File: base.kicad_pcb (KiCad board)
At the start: 2 copper layers, 95 x 95 mm, 4 parts, among them M8 MountingHole_8.4mm_M8

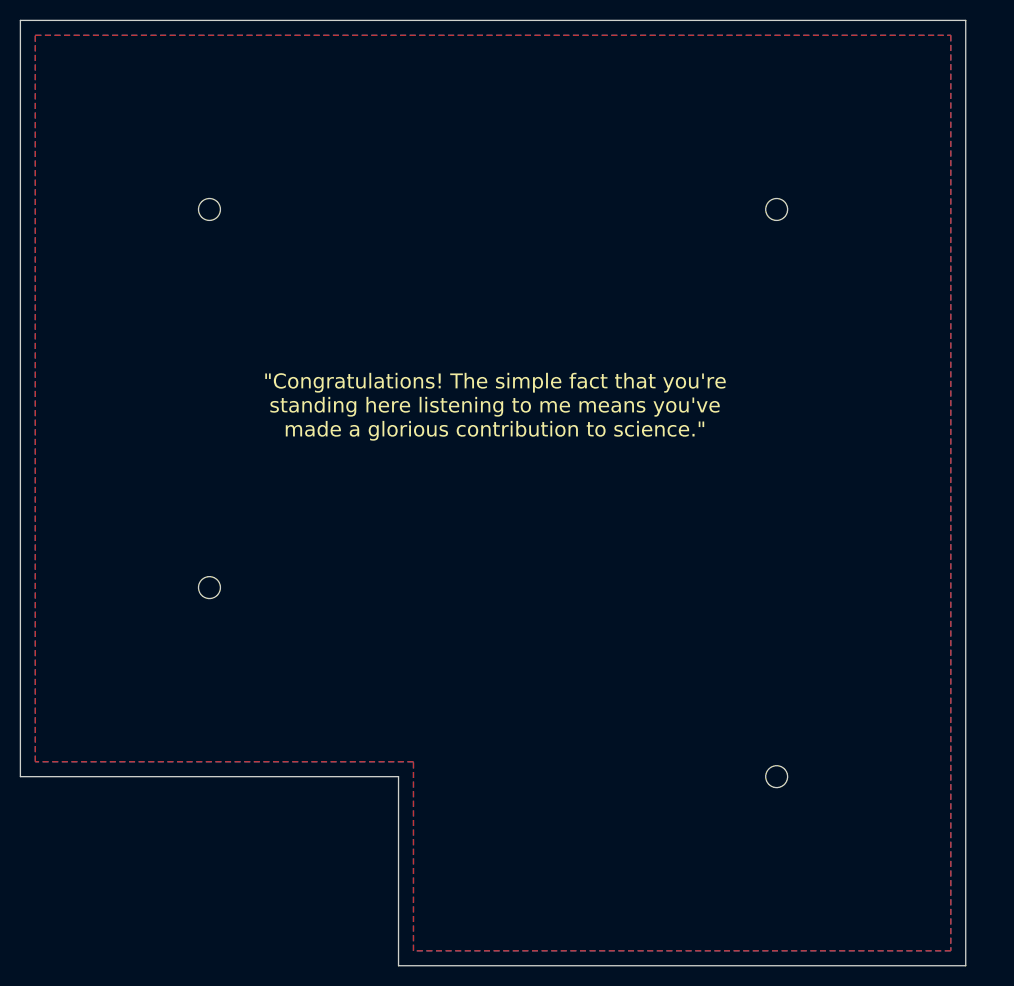
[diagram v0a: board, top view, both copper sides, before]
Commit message: base: Adds OSEG logo and meta-data
* Source (fixed, manual value)
* License (fixed, manual value)
* Version (placeholder, missing replacement method!)
* Version-Date (placeholder, missing replacement method!)
* Manufacturer (fixed, manual value)
* Manufacturer-Serial-Number (placeholder, filled in by manufacturer)
* Batch (fixed, manual value)
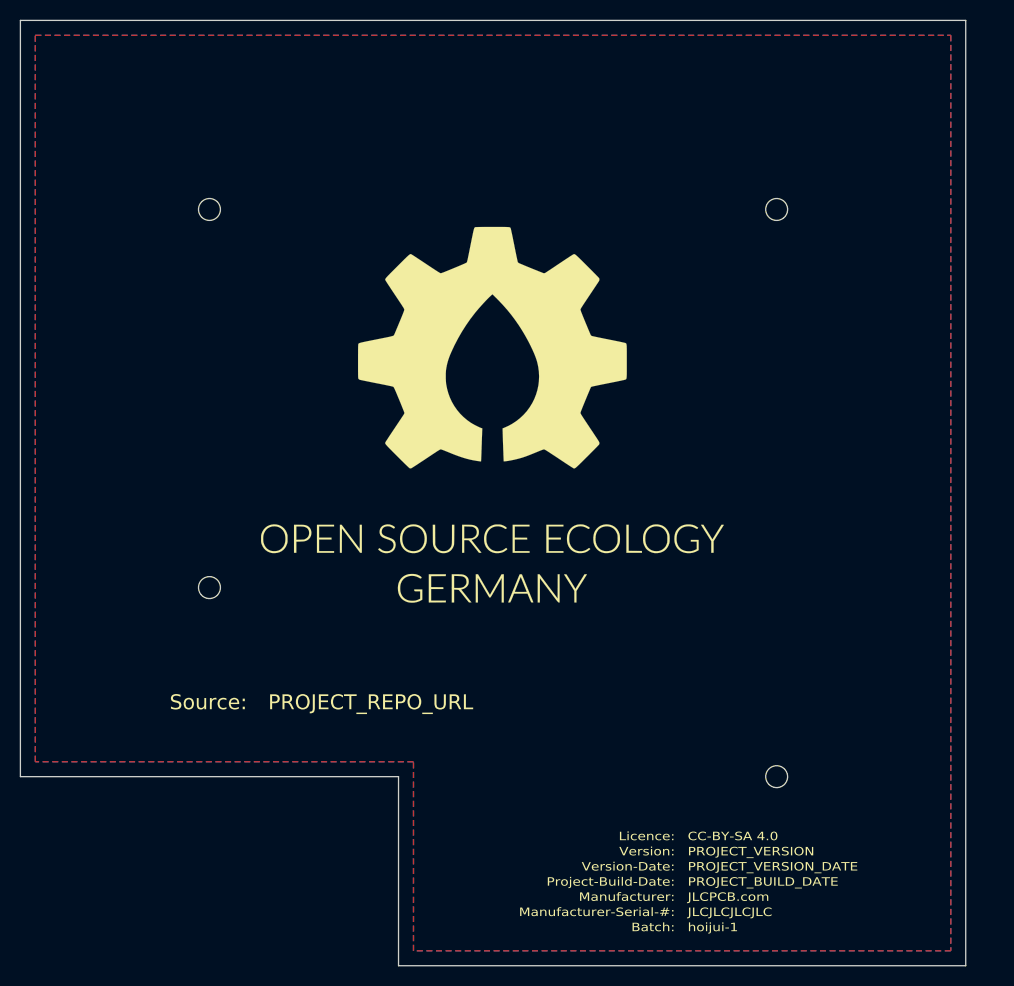
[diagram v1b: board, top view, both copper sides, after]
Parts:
- added G***: LOGO, LOGO, B.Cu at (128.0, 92.7)
- added G***: LOGO, LOGO, F.Cu at (125.7, 88.9)
- added G***: LOGO, LOGO, F.Cu at (126.0, 92.7)
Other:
- rule pad_to_mask_clearance: 0 -> 0.2
- board text added: "Batch:"
- board text added: "CC-BY-SA 4.0"
- board text added: "JLCJLCJLCJLC"
- board text added: "JLCPCB.com"
- board text added: "Licence:"
- board text added: "Manufacturer-Serial-#:"
- board text added: "Manufacturer:"
- board text added: "PROJECT_BUILD_DATE"
- board text added: "PROJECT_REPO_URL"
- board text added: "PROJECT_VERSION"
- board text added: "PROJECT_VERSION_DATE"
- board text added: "Project-Build-Date:"
- board text added: "Source:"
- board text added: "Version-Date:"
- board text added: "Version:"
- board text added: "hoijui-1"
- board text removed: ""Congratulations! The simple fact that you're standing here listening to me means you've made a glorious contribution to science.""

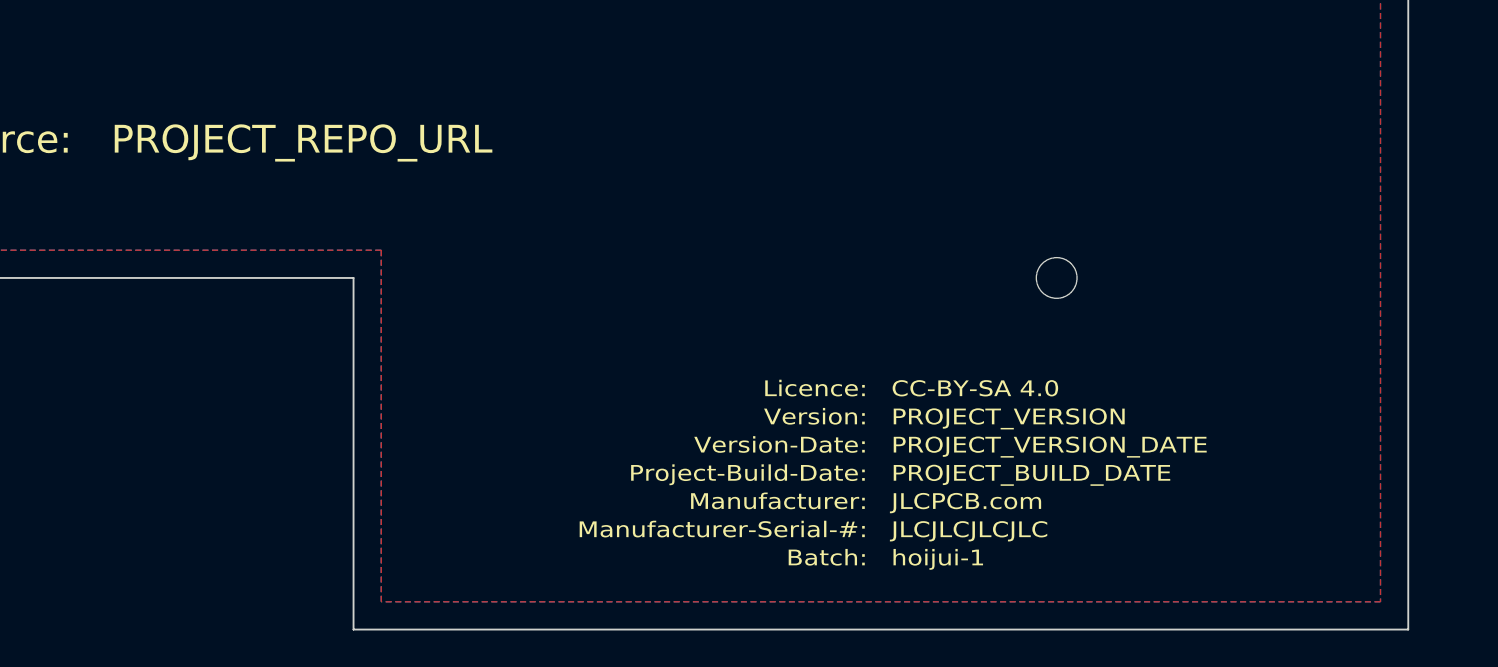
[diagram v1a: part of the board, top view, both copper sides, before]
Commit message: base: Adds more meta-data varables
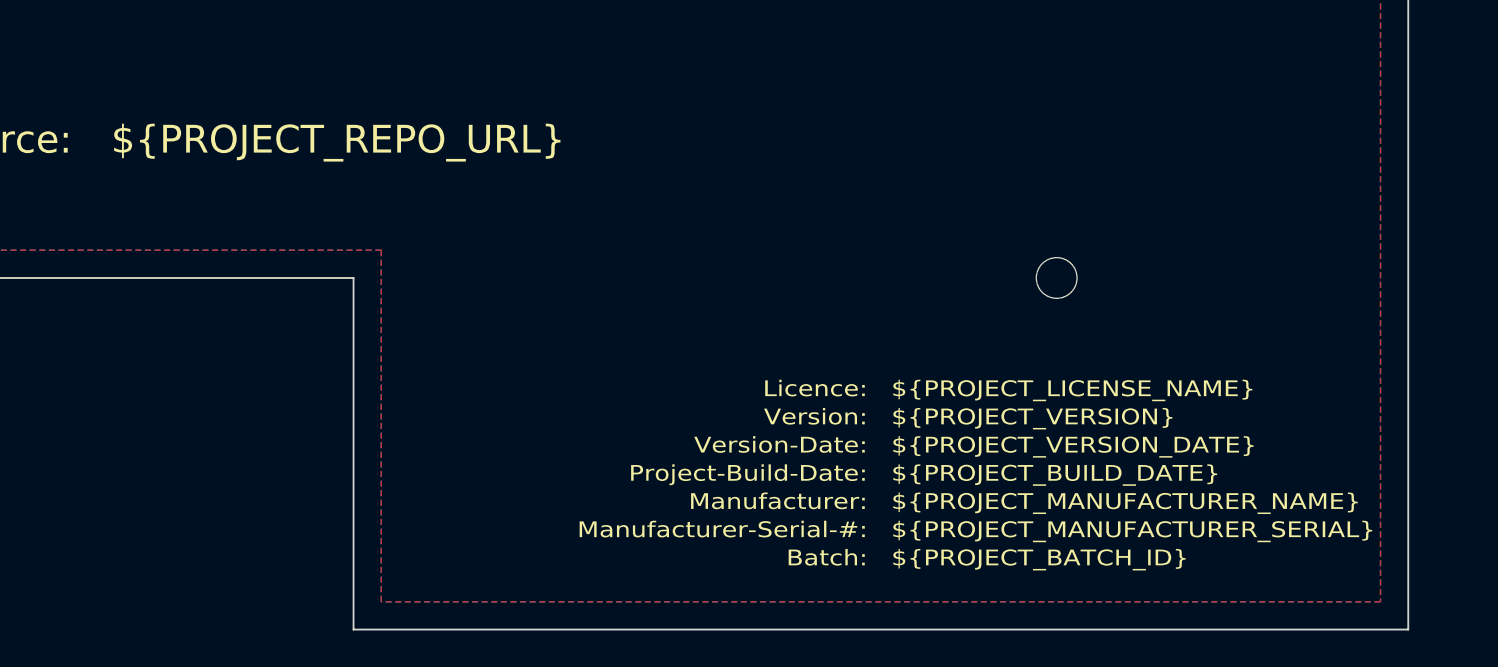
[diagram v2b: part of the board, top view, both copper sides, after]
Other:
- board text added: "${PROJECT_BATCH_ID}"
- board text added: "${PROJECT_BUILD_DATE}"
- board text added: "${PROJECT_LICENSE_NAME}"
- board text added: "${PROJECT_MANUFACTURER_NAME}"
- board text added: "${PROJECT_MANUFACTURER_SERIAL}"
- board text added: "${PROJECT_REPO_URL}"
- board text added: "${PROJECT_VERSION_DATE}"
- board text added: "${PROJECT_VERSION}"
- board text removed: "CC-BY-SA 4.0"
- board text removed: "JLCJLCJLCJLC"
- board text removed: "JLCPCB.com"
- board text removed: "PROJECT_BUILD_DATE"
- board text removed: "PROJECT_REPO_URL"
- board text removed: "PROJECT_VERSION"
- board text removed: "PROJECT_VERSION_DATE"
- board text removed: "hoijui-1"
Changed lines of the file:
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@@
       (xy -7.283727 7.423656) (xy -7.129825 7.419251) (xy -6.975334 7.422964)) (layer F.SilkS) (width 0.01))
   )
-  (gr_text hoijui-1 (at 145.288 135.636) (layer B.SilkS)
+  (gr_text ${PROJECT_BATCH_ID} (at 145.288 135.636) (layer B.SilkS)
     (effects (font (size 0.85 1) (thickness 0.15)) (justify left mirror))
   )
@@
     (effects (font (size 0.85 1) (thickness 0.15)) (justify right mirror))
   )
-  (gr_text hoijui-1 (at 146.558 135.636) (layer F.SilkS)
+  (gr_text ${PROJECT_BATCH_ID} (at 146.558 135.636) (layer F.SilkS)
     (effects (font (size 0.85 1) (thickness 0.15)) (justify left))
   )
@@
     (effects (font (size 0.85 1) (thickness 0.15)) (justify right))
   )
-  (gr_text PROJECT_REPO_URL (at 151.13 113.03) (layer B.SilkS)
+  (gr_text ${PROJECT_REPO_URL} (at 151.13 113.03) (layer B.SilkS)
     (effects (font (size 1.5 1.5) (thickness 0.25)) (justify left mirror))
   )
-  (gr_text PROJECT_REPO_URL (at 104.394 113.03) (layer F.SilkS)
+  (gr_text ${PROJECT_REPO_URL} (at 104.394 113.03) (layer F.SilkS)
     (effects (font (size 1.5 1.5) (thickness 0.25)) (justify left))
   )
-  (gr_text JLCJLCJLCJLC (at 145.288 134.112) (layer B.SilkS)
+  (gr_text ${PROJECT_MANUFACTURER_SERIAL} (at 145.288 134.112) (layer B.SilkS)
     (effects (font (size 0.85 1) (thickness 0.15)) (justify left mirror))
   )
-  (gr_text PROJECT_VERSION_DATE (at 145.288 129.54) (layer B.SilkS)
+  (gr_text ${PROJECT_VERSION_DATE} (at 145.288 129.54) (layer B.SilkS)
     (effects (font (size 0.85 1) (thickness 0.15)) (justify left mirror))
   )
@@
     (effects (font (size 0.85 1) (thickness 0.15)) (justify right mirror))
   )
-  (gr_text PROJECT_VERSION (at 145.288 128.016) (layer B.SilkS)
+  (gr_text ${PROJECT_VERSION} (at 145.288 128.016) (layer B.SilkS)
     (effects (font (size 0.85 1) (thickness 0.15)) (justify left mirror))
   )
-  (gr_text PROJECT_BUILD_DATE (at 145.288 131.064) (layer B.SilkS)
+  (gr_text ${PROJECT_BUILD_DATE} (at 145.288 131.064) (layer B.SilkS)
     (effects (font (size 0.85 1) (thickness 0.15)) (justify left mirror))
   )
-  (gr_text JLCPCB.com (at 145.288 132.588) (layer B.SilkS)
+  (gr_text ${PROJECT_MANUFACTURER_NAME} (at 145.288 132.588) (layer B.SilkS)
     (effects (font (size 0.85 1) (thickness 0.15)) (justify left mirror))
   )
@@
     (effects (font (size 0.85 1) (thickness 0.15)) (justify right mirror))
   )
-  (gr_text "CC-BY-SA 4.0" (at 145.288 126.492) (layer B.SilkS)
+  (gr_text "${PROJECT_LICENSE_NAME}" (at 145.288 126.492) (layer B.SilkS)
     (effects (font (size 0.85 1) (thickness 0.15)) (justify left mirror))
   )
@@
     (effects (font (size 0.85 1) (thickness 0.15)) (justify right mirror))
   )
-  (gr_text PROJECT_BUILD_DATE (at 146.558 131.064) (layer F.SilkS)
+  (gr_text ${PROJECT_BUILD_DATE} (at 146.558 131.064) (layer F.SilkS)
     (effects (font (size 0.85 1) (thickness 0.15)) (justify left))
   )
@@
     (arrow2b (pts (xy 174.5 141.25) (xy 173.373496 141.836421)))
   )
-  (gr_text JLCJLCJLCJLC (at 146.558 134.112) (layer F.SilkS)
+  (gr_text ${PROJECT_MANUFACTURER_SERIAL}  (at 146.558 134.112) (layer F.SilkS)
     (effects (font (size 0.85 1) (thickness 0.15)) (justify left))
   )
-  (gr_text JLCPCB.com (at 146.558 132.588) (layer F.SilkS)
+  (gr_text ${PROJECT_MANUFACTURER_NAME} (at 146.558 132.588) (layer F.SilkS)
     (effects (font (size 0.85 1) (thickness 0.15)) (justify left))
   )
-  (gr_text PROJECT_VERSION_DATE (at 146.558 129.54) (layer F.SilkS)
+  (gr_text ${PROJECT_VERSION_DATE} (at 146.558 129.54) (layer F.SilkS)
     (effects (font (size 0.85 1) (thickness 0.15)) (justify left))
   )
-  (gr_text PROJECT_VERSION (at 146.558 128.016) (layer F.SilkS)
+  (gr_text ${PROJECT_VERSION} (at 146.558 128.016) (layer F.SilkS)
     (effects (font (size 0.85 1) (thickness 0.15)) (justify left))
   )
@@
     (effects (font (size 0.85 1) (thickness 0.15)) (justify right))
   )
-  (gr_text "CC-BY-SA 4.0" (at 146.558 126.492) (layer F.SilkS)
+  (gr_text ${PROJECT_LICENSE_NAME} (at 146.558 126.492) (layer F.SilkS)
     (effects (font (size 0.85 1) (thickness 0.15)) (justify left))
   )

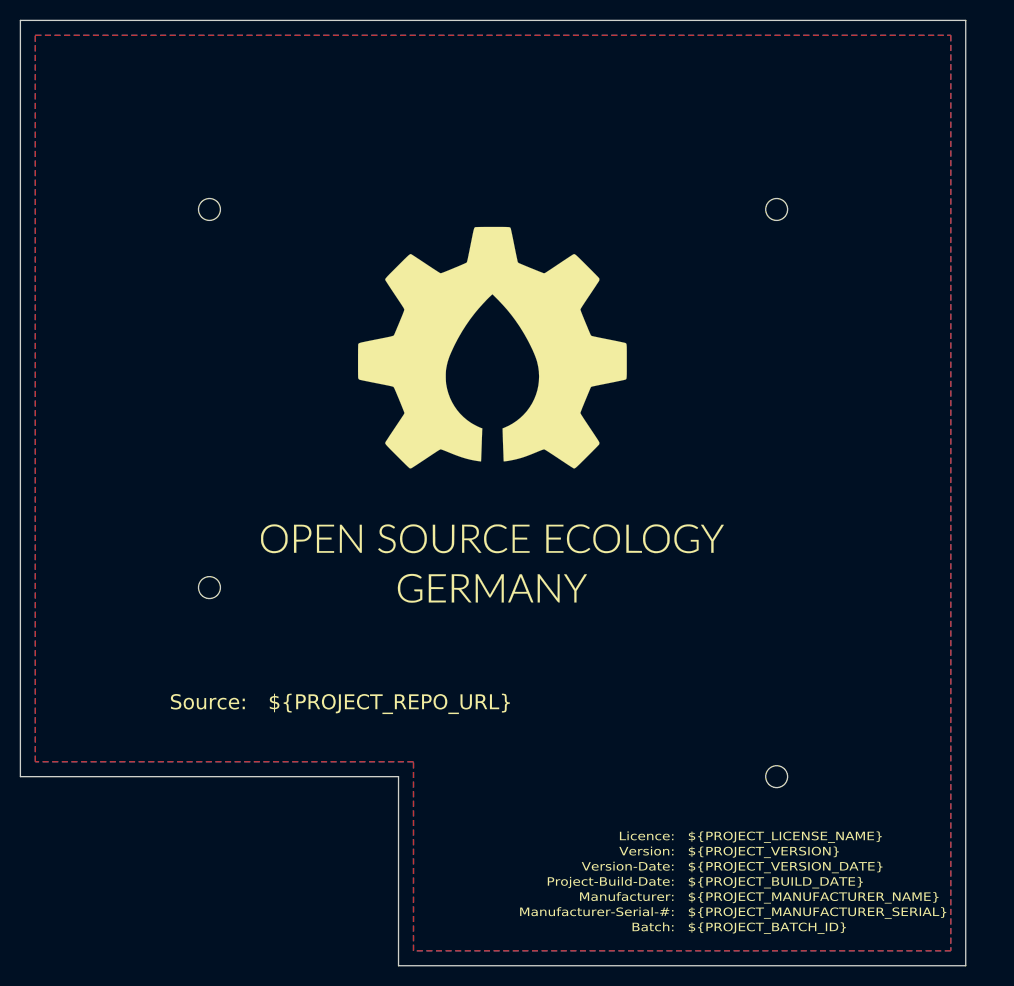
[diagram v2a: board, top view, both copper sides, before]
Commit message: TMP adds 5 rectangles for image injector
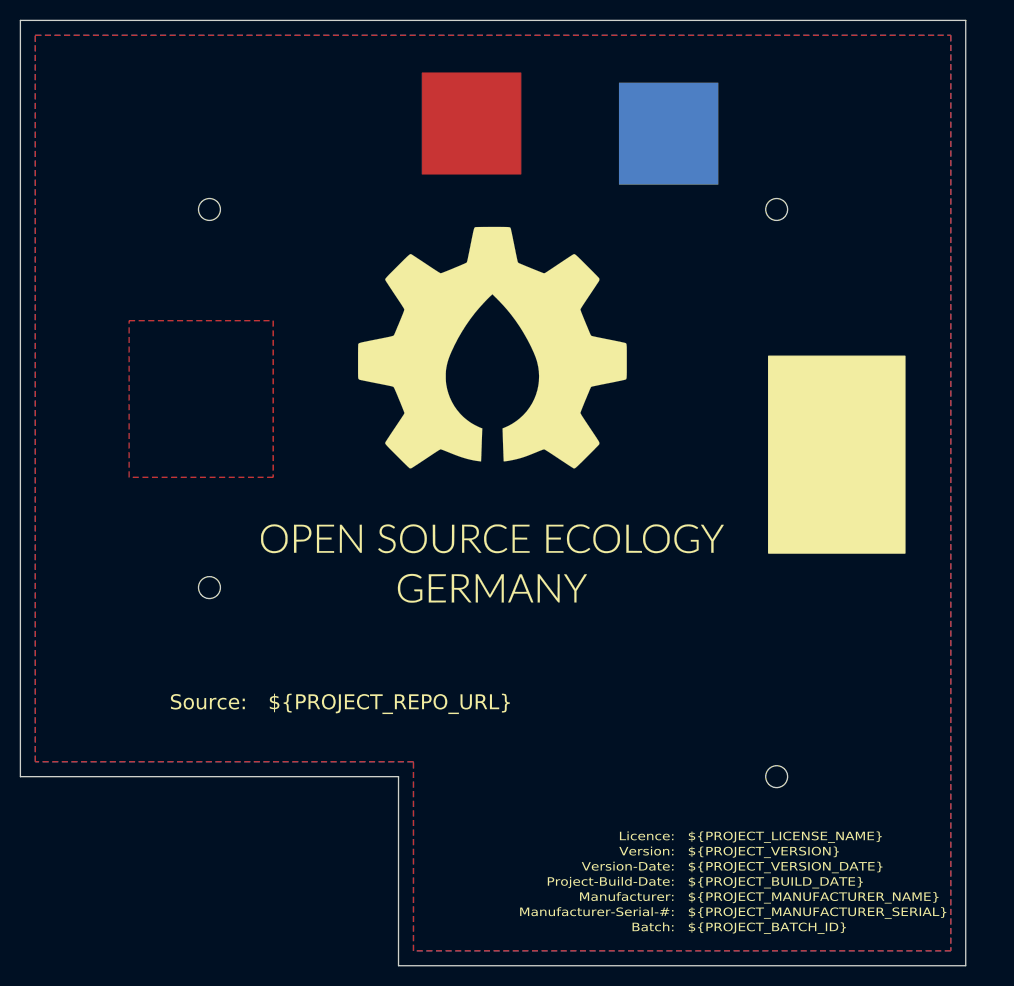
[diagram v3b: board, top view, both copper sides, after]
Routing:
- added copper zone on F.Cu, net (none)
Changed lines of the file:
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@@
-(kicad_pcb (version 20171130) (host pcbnew 5.1.6+dfsg1-1)
+(kicad_pcb (version 20171130) (host pcbnew 5.1.9+dfsg1-1)
   (general
     (thickness 1.6)
-    (drawings 39)
+    (drawings 43)
     (tracks 0)
     (zones 0)
@@
     (34 B.Paste user)
     (35 F.Paste user)
-    (36 B.SilkS user hide)
+    (36 B.SilkS user)
     (37 F.SilkS user)
     (38 B.Mask user)
@@
       (xy -7.283727 7.423656) (xy -7.129825 7.419251) (xy -6.975334 7.422964)) (layer F.SilkS) (width 0.01))
   )
+  (gr_poly (pts (xy 116.332 50.546) (xy 116.332 60.706) (xy 106.426 60.706) (xy 106.426 50.546)) (layer B.SilkS) (width 0.1))
+  (gr_poly (pts (xy 149.606 50.8) (xy 149.606 60.96) (xy 139.7 60.96) (xy 139.7 50.8)) (layer B.Cu) (width 0.1))
+  (gr_poly (pts (xy 129.794 49.784) (xy 129.794 59.944) (xy 119.888 59.944) (xy 119.888 49.784)) (layer F.Cu) (width 0.1))
+  (gr_poly (pts (xy 168.402 98.044) (xy 154.686 98.044) (xy 154.686 78.232) (xy 168.402 78.232)) (layer F.SilkS) (width 0.1))
   (gr_text ${PROJECT_BATCH_ID} (at 145.288 135.636) (layer B.SilkS)
     (effects (font (size 0.85 1) (thickness 0.15)) (justify left mirror))
@@
     (effects (font (size 0.85 1) (thickness 0.15)) (justify right mirror))
   )
-  (gr_text "${PROJECT_LICENSE_NAME}" (at 145.288 126.492) (layer B.SilkS)
+  (gr_text ${PROJECT_LICENSE_NAME} (at 145.288 126.492) (layer B.SilkS)
     (effects (font (size 0.85 1) (thickness 0.15)) (justify left mirror))
   )
@@
     (arrow2b (pts (xy 174.5 141.25) (xy 173.373496 141.836421)))
   )
-  (gr_text ${PROJECT_MANUFACTURER_SERIAL}  (at 146.558 134.112) (layer F.SilkS)
+  (gr_text ${PROJECT_MANUFACTURER_SERIAL} (at 146.558 134.112) (layer F.SilkS)
     (effects (font (size 0.85 1) (thickness 0.15)) (justify left))
   )
@@
       )
     )
+  )
+  (zone (net 0) (net_name "") (layer F.Cu) (hatch edge 0.508)
+    (connect_pads (clearance 0.508))
+    (min_thickness 0.254)
+    (fill yes (arc_segments 32) (thermal_gap 0.508) (thermal_bridge_width 0.508))
+    (polygon
+      (pts
+        (xy 104.902 74.676) (xy 104.902 90.424) (xy 90.424 90.424) (xy 90.424 74.676)
+      )
+    )
